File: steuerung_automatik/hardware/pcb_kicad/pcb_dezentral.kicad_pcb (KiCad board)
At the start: 2 copper layers, 37 parts, among them J1 USB_C_Receptacle_USB2.0, SW1 SW_MEC_5E, SW2 SW_MEC_5E, U1 RP2040, U2 W25Q128JVS, U3 AMS1117-3.3, Y1 Crystal_GND24_Small

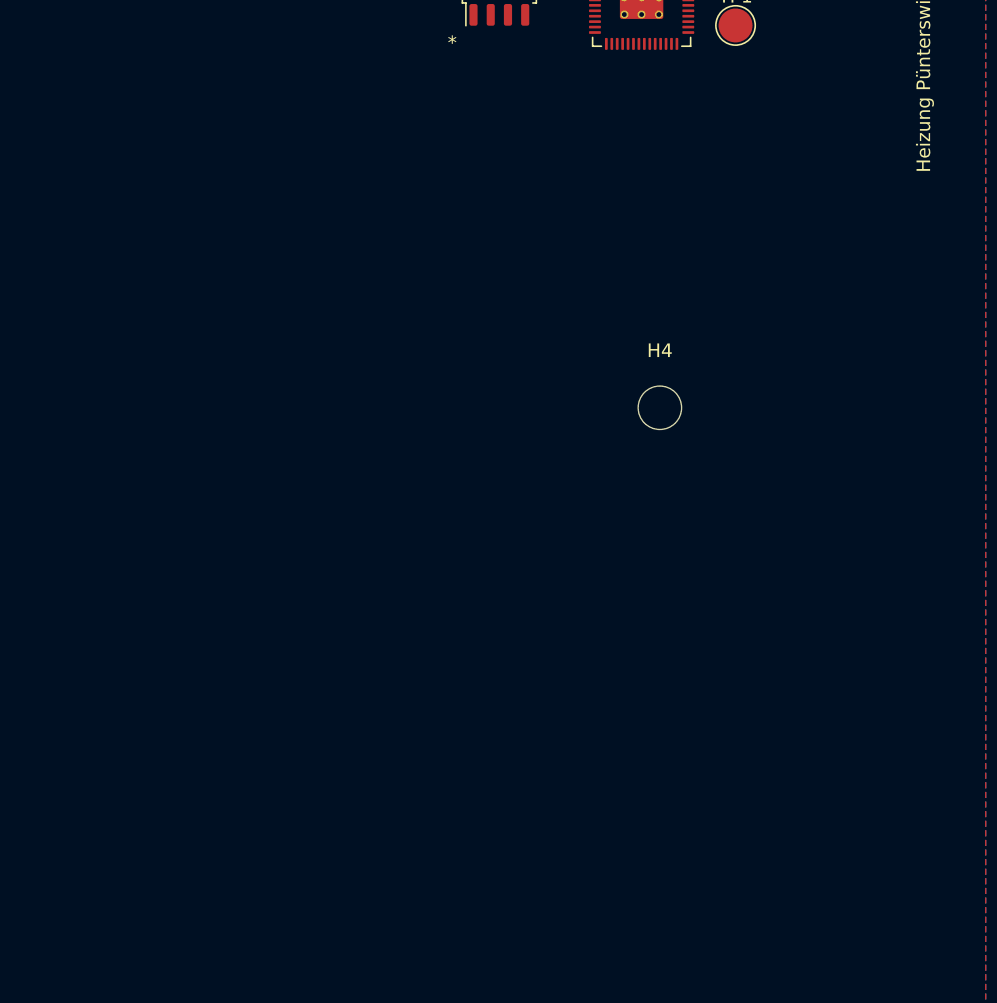
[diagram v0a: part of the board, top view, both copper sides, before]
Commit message: Added footprints
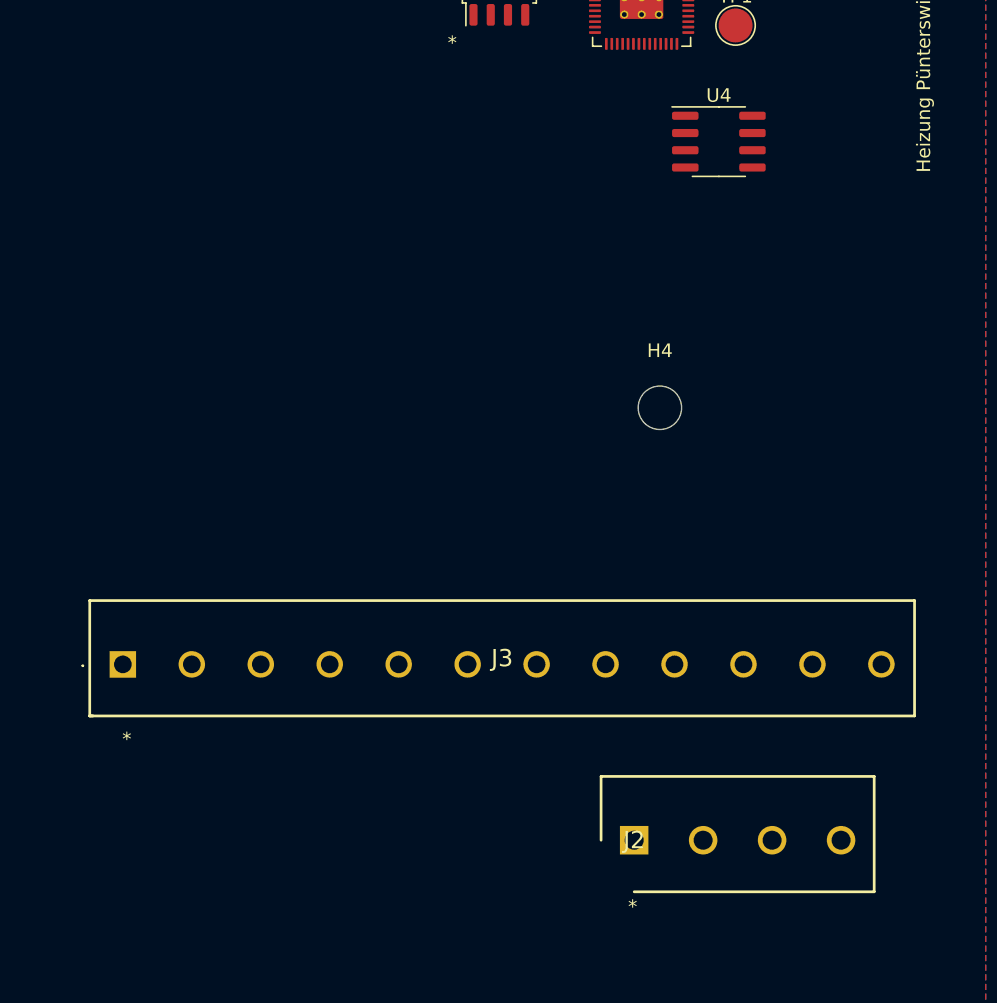
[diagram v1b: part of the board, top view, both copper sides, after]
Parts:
- added J2: weidmueller_SL 5.08HC-04-180, 00_project_library:weidmueller_SL 5.08HC-04-180, F.Cu at (122.1, 141.9)
- added J3: weidmueller_SL 5.08HC-12-180, 00_project_library:weidmueller_SL 5.08HC-12-180, F.Cu at (84.4, 128.9)
- added U4: SP3485EN-L/TR, Package_SO:SOIC-8_3.9x4.9mm_P1.27mm, F.Cu at (128.3, 90.4)

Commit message: Nach Review
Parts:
- removed C1, C10, C11, C12, C13, C14, C2, C5, C6, C9: 100n, Capacitor_SMD:C_0402_1005Metric_Pad0.74x0.62mm_HandSolder
- removed C15, C16: 10u, Capacitor_SMD:C_0603_1608Metric
- removed C3, C4: 1u, Capacitor_SMD:C_0402_1005Metric_Pad0.74x0.62mm_HandSolder
- removed C7, C8: 30p, Capacitor_SMD:C_0402_1005Metric
- removed D1: LED GREEN, 00_project_library:LED_0603_1608Metric
- removed J2: weidmueller_SL 5.08HC-04-180, 00_project_library:weidmueller_SL 5.08HC-04-180
- removed J3: weidmueller_SL 5.08HC-12-180, 00_project_library:weidmueller_SL 5.08HC-12-180
- removed R1, R2: 5.1K, Resistor_SMD:R_0402_1005Metric_Pad0.72x0.64mm_HandSolder
- removed R3, R4: 27R, Resistor_SMD:R_0402_1005Metric_Pad0.72x0.64mm_HandSolder
- removed R5, R7: 10K, Resistor_SMD:R_0402_1005Metric_Pad0.72x0.64mm_HandSolder
- removed R6: 470R, Resistor_SMD:R_0402_1005Metric_Pad0.72x0.64mm_HandSolder
- removed R8: 1k, Resistor_SMD:R_0402_1005Metric_Pad0.72x0.64mm_HandSolder
- removed SW1, SW2: SW_MEC_5E, 00_project_library:SW_TS-1187A-B-A-B
- removed TP1: TestPoint, TestPoint:TestPoint_Pad_D2.5mm
- removed U1: RP2040, 00_project_library:RP2040-QFN-56
- removed U2: W25Q128JVS, 00_project_library:SOIC-8_5.23x5.23mm_P1.27mm
- removed U3: AMS1117-3.3, 00_project_library:SOT-223-3_TabPin2
- removed U4: SP3485EN-L/TR, Package_SO:SOIC-8_3.9x4.9mm_P1.27mm
- removed Y1: Crystal_GND24_Small, 00_project_library:Crystal_SMD_3225-4Pin_3.2x2.5mm
- added C101: 100n, Capacitor_SMD:C_0402_1005Metric_Pad0.74x0.62mm_HandSolder, F.Cu at (134.6, 137.4)
- added C102: 100n, Capacitor_SMD:C_0402_1005Metric_Pad0.74x0.62mm_HandSolder, F.Cu at (134.6, 139.3)
- added C103: 1u, Capacitor_SMD:C_0402_1005Metric_Pad0.74x0.62mm_HandSolder, F.Cu at (134.6, 141.3)
- added C104: 1u, Capacitor_SMD:C_0402_1005Metric_Pad0.74x0.62mm_HandSolder, F.Cu at (134.6, 143.3)
- added C105: 100n, Capacitor_SMD:C_0402_1005Metric_Pad0.74x0.62mm_HandSolder, F.Cu at (137.8, 137.4)
- added C106: 100n, Capacitor_SMD:C_0402_1005Metric_Pad0.74x0.62mm_HandSolder, F.Cu at (137.8, 139.3)
- added C107: 30p, Capacitor_SMD:C_0402_1005Metric, F.Cu at (121.9, 153.3)
- added C108: 30p, Capacitor_SMD:C_0402_1005Metric, F.Cu at (121.9, 155.2)
- added C109: 100n, Capacitor_SMD:C_0402_1005Metric_Pad0.74x0.62mm_HandSolder, F.Cu at (137.8, 141.3)
- added C110: 100n, Capacitor_SMD:C_0402_1005Metric_Pad0.74x0.62mm_HandSolder, F.Cu at (137.8, 143.3)
- added C111: 100n, Capacitor_SMD:C_0402_1005Metric_Pad0.74x0.62mm_HandSolder, F.Cu at (141.0, 137.4)
- added C112: 100n, Capacitor_SMD:C_0402_1005Metric_Pad0.74x0.62mm_HandSolder, F.Cu at (141.0, 139.3)
- added C113: 100n, Capacitor_SMD:C_0402_1005Metric_Pad0.74x0.62mm_HandSolder, F.Cu at (141.0, 141.3)
- added C114: 100n, Capacitor_SMD:C_0402_1005Metric_Pad0.74x0.62mm_HandSolder, F.Cu at (141.0, 143.3)
- added C115: 10u, Capacitor_SMD:C_0603_1608Metric, F.Cu at (140.2, 145.5)
- added C116: 10u, Capacitor_SMD:C_0603_1608Metric, F.Cu at (140.2, 148.0)
- added D101: LED GREEN, 00_project_library:LED_0603_1608Metric, F.Cu at (140.7, 131.9)
- added H101: MountingHole, MountingHole:MountingHole_3.2mm_M3, F.Cu at (106.7, 125.2)
- added H102: MountingHole, MountingHole:MountingHole_3.2mm_M3, F.Cu at (106.7, 133.2)
- added H103: MountingHole, MountingHole:MountingHole_3.2mm_M3, F.Cu at (106.7, 141.1)
- added H104: MountingHole, MountingHole:MountingHole_3.2mm_M3, F.Cu at (106.7, 149.1)
- added J101: USB_C_Receptacle_USB2.0, 00_project_library:USB_C_Receptacle_Palconn_UTC16-G, F.Cu at (129.5, 153.8)
- added J102: weidmueller_SL5.08HC-04-90, 00_project_library:weidmueller_SL5.08HC-04-90, F.Cu at (127.5, 94.1)
- added J103: weidmueller_SL5.08HC-12-90, 00_project_library:weidmueller_SL5.08HC-12-90, F.Cu at (62.4, 92.3)
- added R101: 5.1K, Resistor_SMD:R_0402_1005Metric_Pad0.72x0.64mm_HandSolder, F.Cu at (122.1, 137.4)
- added R102: 5.1K, Resistor_SMD:R_0402_1005Metric_Pad0.72x0.64mm_HandSolder, F.Cu at (122.1, 139.4)
- added R103: 27R, Resistor_SMD:R_0402_1005Metric_Pad0.72x0.64mm_HandSolder, F.Cu at (122.1, 141.3)
- added R104: 27R, Resistor_SMD:R_0402_1005Metric_Pad0.72x0.64mm_HandSolder, F.Cu at (122.1, 143.3)
- added R105: 10K, Resistor_SMD:R_0402_1005Metric_Pad0.72x0.64mm_HandSolder, F.Cu at (122.1, 145.3)
- added R106: 470R, Resistor_SMD:R_0402_1005Metric_Pad0.72x0.64mm_HandSolder, F.Cu at (122.1, 147.3)
- added R107: 10K, Resistor_SMD:R_0402_1005Metric_Pad0.72x0.64mm_HandSolder, F.Cu at (122.1, 149.3)
- added R108: 1k, Resistor_SMD:R_0402_1005Metric_Pad0.72x0.64mm_HandSolder, F.Cu at (122.1, 151.3)
- added SW101: SW_MEC_5E, 00_project_library:SW_TS-1187A-B-A-B, F.Cu at (128.7, 139.7)
- added SW102: SW_MEC_5E, 00_project_library:SW_TS-1187A-B-A-B, F.Cu at (128.7, 146.3)
- added TP101: TestPoint, TestPoint:TestPoint_Pad_D2.5mm, F.Cu at (136.3, 132.8)
- added U101: RP2040, 00_project_library:RP2040-QFN-56, F.Cu at (138.7, 125.9)
- added U102: W25Q128JVS, 00_project_library:SOIC-8_5.23x5.23mm_P1.27mm, F.Cu at (115.6, 140.5)
- added U103: SP3485EN-L/TR, Package_SO:SOIC-8_3.9x4.9mm_P1.27mm, F.Cu at (138.7, 154.8)
- added U104: AMS1117-3.3, 00_project_library:SOT-223-3_TabPin2, F.Cu at (114.9, 156.1)
- added Y101: Crystal_GND24_Small, 00_project_library:Crystal_SMD_3225-4Pin_3.2x2.5mm, F.Cu at (135.6, 146.5)

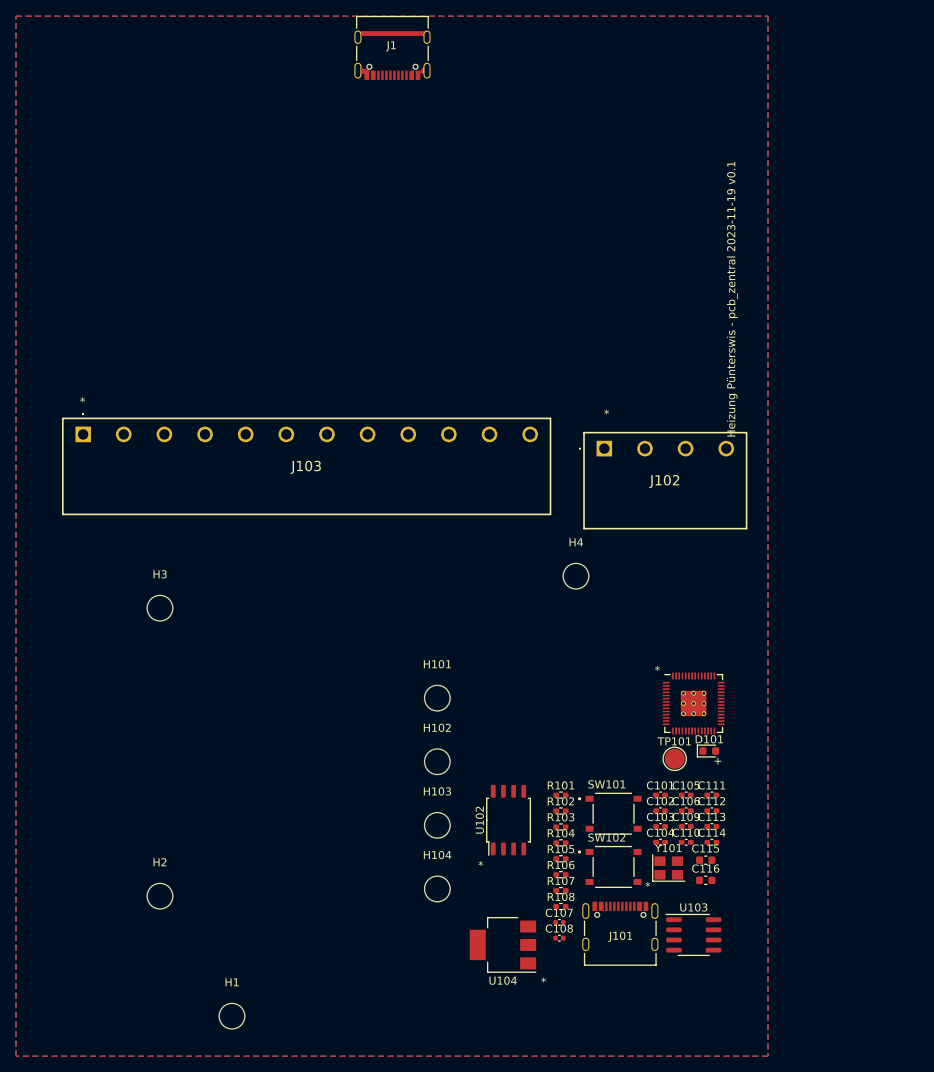
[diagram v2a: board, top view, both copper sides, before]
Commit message: Add weidmueller and din_rail_pcb_holder footprints
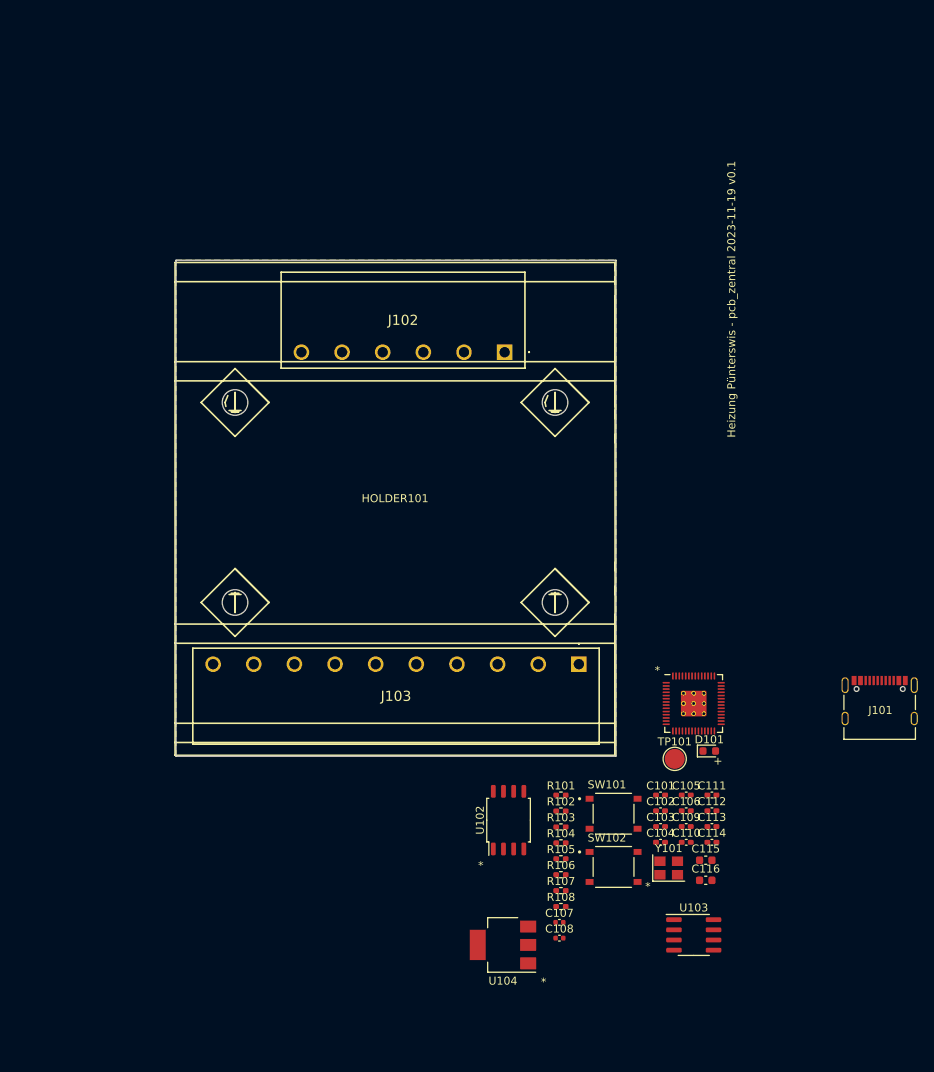
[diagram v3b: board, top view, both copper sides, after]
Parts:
- removed H1, H101, H102, H103, H104, H2, H3, H4: MountingHole, MountingHole:MountingHole_3.2mm_M3
- removed J1: USB_C_Receptacle_USB2.0, 00_project_library:USB_C_Receptacle_Palconn_UTC16-G
- added HOLDER101: ~, 00_project_library:din_rail_pcb_holder, F.Cu at (101.4, 100.8)
- J102: value weidmueller_SL5.08HC-04-90 -> weidmueller_SL5.08HC-06-90; footprint 00_project_library:weidmueller_SL5.08HC-04-90 -> 00_project_library:weidmueller_SL5.08HC-06-90
- J103: value weidmueller_SL5.08HC-12-90 -> weidmueller_SL5.08HC-10-90; footprint 00_project_library:weidmueller_SL5.08HC-12-90 -> 00_project_library:weidmueller_SL5.08HC-10-90
- moved J103 68.3 mm to (124.4, 121.0)
- moved J101 43.0 mm to (162.0, 125.5)
- moved J102 17.3 mm to (115.1, 82.0), turned to 180 degrees
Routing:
- net GND: track 10.8 -> 0.00 mm
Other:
- board outline added: 55 x 62 mm

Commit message: Schema dezentral komplett
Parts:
- removed C101, C102, C105, C106, C109, C110, C111, C112, C113, C114: 100n, Capacitor_SMD:C_0402_1005Metric_Pad0.74x0.62mm_HandSolder
- removed C103, C104: 1u, Capacitor_SMD:C_0402_1005Metric_Pad0.74x0.62mm_HandSolder
- removed C107, C108: 30p, Capacitor_SMD:C_0402_1005Metric
- removed C115, C116: 10u, Capacitor_SMD:C_0603_1608Metric
- removed D101: LED GREEN, 00_project_library:LED_0603_1608Metric
- removed HOLDER101: ~, 00_project_library:din_rail_pcb_holder
- removed J101: USB_C_Receptacle_USB2.0, 00_project_library:USB_C_Receptacle_Palconn_UTC16-G
- removed J102: weidmueller_SL5.08HC-06-90, 00_project_library:weidmueller_SL5.08HC-06-90
- removed J103: weidmueller_SL5.08HC-10-90, 00_project_library:weidmueller_SL5.08HC-10-90
- removed R101, R102: 5.1K, Resistor_SMD:R_0402_1005Metric_Pad0.72x0.64mm_HandSolder
- removed R103, R104: 27R, Resistor_SMD:R_0402_1005Metric_Pad0.72x0.64mm_HandSolder
- removed R105, R107: 10K, Resistor_SMD:R_0402_1005Metric_Pad0.72x0.64mm_HandSolder
- removed R106: 470R, Resistor_SMD:R_0402_1005Metric_Pad0.72x0.64mm_HandSolder
- removed R108: 1k, Resistor_SMD:R_0402_1005Metric_Pad0.72x0.64mm_HandSolder
- removed SW101, SW102: SW_MEC_5E, 00_project_library:SW_TS-1187A-B-A-B
- removed TP101: TestPoint, TestPoint:TestPoint_Pad_D2.5mm
- removed U101: RP2040, 00_project_library:RP2040-QFN-56
- removed U102: W25Q128JVS, 00_project_library:SOIC-8_5.23x5.23mm_P1.27mm
- removed U103: SP3485EN-L/TR, Package_SO:SOIC-8_3.9x4.9mm_P1.27mm
- removed U104: AMS1117-3.3, 00_project_library:SOT-223-3_TabPin2
- removed Y101: Crystal_GND24_Small, 00_project_library:Crystal_SMD_3225-4Pin_3.2x2.5mm
- added C1: 4u7 50V, Diode_SMD:D_1206_3216Metric, F.Cu at (126.4, 106.3)
- added C2: 100n 50V, Diode_SMD:D_0805_2012Metric, F.Cu at (126.5, 108.9)
- added C3: 100n 50V, Diode_SMD:D_0805_2012Metric, F.Cu at (119.4, 106.3)
- added C4: 10u 25V, Diode_SMD:D_0805_2012Metric, F.Cu at (124.0, 99.3)
- added C5: 100n 50V, Diode_SMD:D_0805_2012Metric, F.Cu at (124.0, 97.0)
- added C6: 100n 50V, Diode_SMD:D_0805_2012Metric, F.Cu at (121.8, 69.5)
- added C901: 10u, Capacitor_SMD:C_0603_1608Metric, F.Cu at (87.7, 123.3)
- added C902: 10u, Capacitor_SMD:C_0603_1608Metric, F.Cu at (92.6, 123.3)
- added C903: 100n, Capacitor_SMD:C_0402_1005Metric_Pad0.74x0.62mm_HandSolder, F.Cu at (247.9, 121.8)
- added C904: 100n, Capacitor_SMD:C_0402_1005Metric_Pad0.74x0.62mm_HandSolder, F.Cu at (247.9, 123.8)
- added C905: 1u, Capacitor_SMD:C_0402_1005Metric_Pad0.74x0.62mm_HandSolder, F.Cu at (247.9, 125.7)
- added C906: 1u, Capacitor_SMD:C_0402_1005Metric_Pad0.74x0.62mm_HandSolder, F.Cu at (247.9, 127.7)
- added C907: 100n, Capacitor_SMD:C_0402_1005Metric_Pad0.74x0.62mm_HandSolder, F.Cu at (251.1, 121.8)
- added C908: 100n, Capacitor_SMD:C_0402_1005Metric_Pad0.74x0.62mm_HandSolder, F.Cu at (251.1, 123.8)
- added C909: 30p, Capacitor_SMD:C_0402_1005Metric, F.Cu at (88.1, 95.6)
- added C910: 30p, Capacitor_SMD:C_0402_1005Metric, F.Cu at (85.3, 95.6)
- added C911: 100n, Capacitor_SMD:C_0402_1005Metric_Pad0.74x0.62mm_HandSolder, F.Cu at (251.1, 125.7)
- added C912: 100n, Capacitor_SMD:C_0402_1005Metric_Pad0.74x0.62mm_HandSolder, F.Cu at (251.1, 127.7)
- added C913: 100n, Capacitor_SMD:C_0402_1005Metric_Pad0.74x0.62mm_HandSolder, F.Cu at (254.3, 121.8)
- added C914: 100n, Capacitor_SMD:C_0402_1005Metric_Pad0.74x0.62mm_HandSolder, F.Cu at (254.3, 123.8)
- added C915: 100n, Capacitor_SMD:C_0402_1005Metric_Pad0.74x0.62mm_HandSolder, F.Cu at (254.3, 125.7)
- added C916: 100n, Capacitor_SMD:C_0402_1005Metric_Pad0.74x0.62mm_HandSolder, F.Cu at (254.3, 127.7)
- added D1: B5819W SL, Diode_SMD:D_SOD-123, F.Cu at (76.7, 71.5)
- added D10: B5819W SL, Diode_SMD:D_SOD-123, F.Cu at (96.9, 76.1)
- added D11: B5819W SL, Diode_SMD:D_SOD-123, F.Cu at (102.0, 71.3)
- added D12: B5819W SL, Diode_SMD:D_SOD-123, F.Cu at (102.0, 76.1)
- added D13: B5819W SL, Diode_SMD:D_SOD-123, F.Cu at (107.1, 71.4)
- added D14: B5819W SL, Diode_SMD:D_SOD-123, F.Cu at (107.1, 76.1)
- added D15: B5819W SL, Diode_SMD:D_SOD-123, F.Cu at (112.2, 71.3)
- added D16: B5819W SL, Diode_SMD:D_SOD-123, F.Cu at (112.2, 76.1)
- added D17: SMBJ30A, Diode_SMD:D_SMA, F.Cu at (112.6, 118.7)
- added D18: LED WHITE, 00_project_library:LED_0603_1608Metric, F.Cu at (213.8, 111.8)
- added D19: B5819W SL, Diode_SMD:D_SOD-123, F.Cu at (123.0, 118.7)
- added D2: B5819W SL, Diode_SMD:D_SOD-123, F.Cu at (76.7, 76.2)
- added D20: B5819W SL, Diode_SMD:D_SOD-123, F.Cu at (233.8, 97.1)
- added D21: SMBJ6.5CA, Diode_SMD:D_SMB, F.Cu at (240.9, 91.5)
- added D22: SMBJ6.5CA, Diode_SMD:D_SMB, F.Cu at (240.9, 97.1)
- added D23: SMBJ6.5CA, Diode_SMD:D_SMB, F.Cu at (240.9, 102.6)
- added D24: B5819W SL, Diode_SMD:D_SOD-123, F.Cu at (116.8, 106.6)
- added D25: B5819W SL, Diode_SMD:D_SOD-123, F.Cu at (112.7, 114.3)
- added D3: B5819W SL, Diode_SMD:D_SOD-123, F.Cu at (81.7, 71.4)
- added D4: B5819W SL, Diode_SMD:D_SOD-123, F.Cu at (81.7, 76.1)
- added D5: B5819W SL, Diode_SMD:D_SOD-123, F.Cu at (86.7, 76.0)
- added D6: B5819W SL, Diode_SMD:D_SOD-123, F.Cu at (86.7, 71.3)
- added D7: B5819W SL, Diode_SMD:D_SOD-123, F.Cu at (91.9, 76.1)
- added D8: B5819W SL, Diode_SMD:D_SOD-123, F.Cu at (91.9, 71.4)
- added D9: B5819W SL, Diode_SMD:D_SOD-123, F.Cu at (96.9, 71.3)
- added D901: LED GREEN, 00_project_library:LED_0603_1608Metric, F.Cu at (106.2, 108.7)
- added D904: B5819W SL, Diode_SMD:D_SOD-123, F.Cu at (83.2, 123.0)
- added HOLDER1: ~, 00_project_library:din_rail_pcb_holder, F.Cu at (101.5, 101.0)
- added J1: weidmueller_SL5.08HC-06-90, 00_project_library:weidmueller_SL5.08HC-06-90, F.Cu at (99.7, 122.5)
- added J2: weidmueller_SL5.08HC-10-90, 00_project_library:weidmueller_SL5.08HC-10-90, F.Cu at (78.4, 65.5)
- added J901: USB_C_Receptacle_USB2.0, 00_project_library:USB_C_Receptacle_Palconn_UTC16-G, F.Cu at (79.9, 127.7)
- added L1: 22uH, 00_project_library:L_MODBUS, F.Cu at (118.8, 100.3)
- added Q1: AO3400A, Package_TO_SOT_SMD:SOT-23, F.Cu at (209.3, 112.7)
- added R1: 4k7, Resistor_SMD:R_0402_1005Metric_Pad0.72x0.64mm_HandSolder, F.Cu at (75.0, 70.3)
- added R10: 10k, Resistor_SMD:R_0402_1005Metric_Pad0.72x0.64mm_HandSolder, F.Cu at (241.5, 114.4)
- added R11: 100k, Resistor_SMD:R_0402_1005Metric_Pad0.72x0.64mm_HandSolder, F.Cu at (125.3, 104.3)
- added R12: 56k, Resistor_SMD:R_0402_1005Metric_Pad0.72x0.64mm_HandSolder, F.Cu at (116.7, 110.1)
- added R13: 10k, Resistor_SMD:R_0402_1005Metric_Pad0.72x0.64mm_HandSolder, F.Cu at (117.7, 110.1)
- added R2: 4k7, Resistor_SMD:R_0402_1005Metric_Pad0.72x0.64mm_HandSolder, F.Cu at (80.1, 70.4)
- added R3: 4k7, Resistor_SMD:R_0402_1005Metric_Pad0.72x0.64mm_HandSolder, F.Cu at (85.1, 70.3)
- added R4: 4k7, Resistor_SMD:R_0402_1005Metric_Pad0.72x0.64mm_HandSolder, F.Cu at (90.3, 70.3)
- added R5: 4k7, Resistor_SMD:R_0402_1005Metric_Pad0.72x0.64mm_HandSolder, F.Cu at (95.3, 70.3)
- added R6: 4k7, Resistor_SMD:R_0402_1005Metric_Pad0.72x0.64mm_HandSolder, F.Cu at (100.3, 70.3)
- added R7: 4k7, Resistor_SMD:R_0402_1005Metric_Pad0.72x0.64mm_HandSolder, F.Cu at (105.5, 70.3)
- added R8: 4k7, Resistor_SMD:R_0402_1005Metric_Pad0.72x0.64mm_HandSolder, F.Cu at (110.6, 70.3)
- added R9: 470, Resistor_SMD:R_0402_1005Metric_Pad0.72x0.64mm_HandSolder, F.Cu at (241.5, 112.4)
- added R901: 5.1K, Resistor_SMD:R_0402_1005Metric_Pad0.72x0.64mm_HandSolder, F.Cu at (79.3, 128.6)
- added R902: 5.1K, Resistor_SMD:R_0402_1005Metric_Pad0.72x0.64mm_HandSolder, F.Cu at (81.0, 127.2)
- added R903: 27R, Resistor_SMD:R_0402_1005Metric_Pad0.72x0.64mm_HandSolder, F.Cu at (84.6, 107.7)
- added R904: 27R, Resistor_SMD:R_0402_1005Metric_Pad0.72x0.64mm_HandSolder, F.Cu at (83.5, 107.7)
- added R905: 470R, Resistor_SMD:R_0402_1005Metric_Pad0.72x0.64mm_HandSolder, F.Cu at (229.4, 133.1)
- added R906: 1K, Resistor_SMD:R_0402_1005Metric_Pad0.72x0.64mm_HandSolder, F.Cu at (94.5, 116.1)
- added R907: 10K, Resistor_SMD:R_0402_1005Metric_Pad0.72x0.64mm_HandSolder, F.Cu at (95.6, 116.1)
- added R908: 1k, Resistor_SMD:R_0402_1005Metric_Pad0.72x0.64mm_HandSolder, F.Cu at (86.8, 96.2)
- added SW1: dip_switch_SPST16, 00_project_library:dip_switch_SPST16, F.Cu at (100.1, 94.0)
- added SW901: SW_MEC_5E, 00_project_library:SW_TS-1187A-B-A-B, F.Cu at (89.8, 118.5)
- added U1: SP3485EN-L/TR, Package_SO:SOIC-8_3.9x4.9mm_P1.27mm, F.Cu at (244.6, 84.7)
- added U2: AOZ1282CI, Package_TO_SOT_SMD:SOT-23-6, F.Cu at (122.3, 106.3)
- added U901: RP2040, 00_project_library:RP2040-QFN-56, F.Cu at (86.9, 101.8)
- added U902: AMS1117-3.3, 00_project_library:SOT-223-3_TabPin2, F.Cu at (90.5, 127.8)
- added U903: W25Q128JVS, 00_project_library:SOIC-8_5.23x5.23mm_P1.27mm, F.Cu at (91.9, 111.9)
- added Y901: Crystal_GND24_Small, 00_project_library:Crystal_SMD_3225-4Pin_3.2x2.5mm, F.Cu at (87.4, 93.3)
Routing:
- net ds_3V3: track 0.00 -> 223.2 mm
- net ds_7: track 0.00 -> 80.6 mm
- net ds_6: track 0.00 -> 75.0 mm
- net ds_5: track 0.00 -> 71.2 mm
- net ds_4: track 0.00 -> 68.2 mm
- net ds_3: track 0.00 -> 65.0 mm, vias 0 -> 1
- net ds_2: track 0.00 -> 60.8 mm, vias 0 -> 1
- net 485_0V: track 0.00 -> 55.7 mm, vias 0 -> 15
- net ds_1: track 0.00 -> 55.6 mm
- net ds_0: track 0.00 -> 51.8 mm
- net +5V: track 0.00 -> 50.9 mm
- net Net-(D25-A): track 0.00 -> 28.5 mm
- net /cpu/USB_D+: track 0.00 -> 23.3 mm, vias 0 -> 2
- net /cpu/USB_D-: track 0.00 -> 22.4 mm, vias 0 -> 2
- net /cpu/QSPI_SS: track 0.00 -> 20.1 mm
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- added copper zone on B.Cu, net 485_0V
- added copper zone on F.Cu, net 485_0V
- removed copper zone on B.Cu, net GND
- removed copper zone on F.Cu, net GND
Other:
- board size 55 x 62 mm -> 55 x 78 mm
